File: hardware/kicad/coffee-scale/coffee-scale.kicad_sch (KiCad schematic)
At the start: 4 parts, among them U1 ESP32-S3, U2 HX711

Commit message: Update Schematic
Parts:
- added J1: Screw_Terminal_01x02, symbol Connector:Screw_Terminal_01x02
- added U4: MCP73831-2-MC, Package_DFN_QFN:DFN-8-1EP_3x2mm_P0.5mm_EP1.7x1.4mm, symbol Battery_Management:MCP73831-2-MC
- BT1: value Battery_Cell -> 3.7V
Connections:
- new net: J1.2 (Pin_2), U4.3 (V_{BAT}), U4.4 (V_{BAT})
- new net: U4.1 (V_{DD}), U4.2 (V_{DD})
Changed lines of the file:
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@@
 	(generator_version "8.0")
 	(paper "A4")
+	(junction
+		(at 41.91 123.19)
+		(diameter 0)
+		(color 0 0 0 0)
+	)
 	(wire
 		(pts
@@
 	(wire
 		(pts
+			(xy 31.75 123.19) (xy 41.91 123.19)
+		)
+		(stroke
+			(width 0)
+			(type default)
+		)
+	)
+	(wire
+		(pts
 			(xy 107.95 80.01) (xy 107.95 64.77)
 		)
@@
 	(wire
 		(pts
+			(xy 41.91 123.19) (xy 64.77 123.19)
+		)
+		(stroke
+			(width 0)
+			(type default)
+		)
+	)
+	(wire
+		(pts
 			(xy 191.77 87.63) (xy 191.77 81.28)
 		)
@@
 			(width 0)
 			(type default)
+		)
+	)
+	(wire
+		(pts
+			(xy 64.77 118.11) (xy 58.42 118.11)
+		)
+		(stroke
+			(width 0)
+			(type default)
+		)
+	)
+	(symbol
+		(lib_id "Connector:Screw_Terminal_01x02")
+		(at 36.83 125.73 180)
+		(unit 1)
+		(exclude_from_sim no)
+		(in_bom yes)
+		(on_board yes)
+		(dnp no)
+		(fields_autoplaced yes)
+		(property "Reference" "J1"
+			(at 36.83 116.84 0)
+			(effects
+				(font
+					(size 1.27 1.27)
+				)
+			)
+		)
+		(property "Value" "Screw_Terminal_01x02"
+			(at 36.83 119.38 0)
+			(effects
+				(font
+					(size 1.27 1.27)
+				)
+			)
+		)
+		(property "Footprint" ""
+			(at 36.83 125.73 0)
+			(effects
+				(font
+					(size 1.27 1.27)
+				)
+				(hide yes)
+			)
+		)
+		(property "Datasheet" "~"
+			(at 36.83 125.73 0)
+			(effects
+				(font
+					(size 1.27 1.27)
+				)
+				(hide yes)
+			)
+		)
+		(property "Description" "Generic screw terminal, single row, 01x02, script generated (kicad-library-utils/schlib/autogen/connector/)"
+			(at 36.83 125.73 0)
+			(effects
+				(font
+					(size 1.27 1.27)
+				)
+				(hide yes)
+			)
+		)
+		(pin "2"
+		)
+		(pin "1"
+		)
+		(instances
+			(project ""
+				(path "/26376108-b2bd-4c81-9164-5810df14cd80"
+					(reference "J1")
+					(unit 1)
+				)
+			)
 		)
 	)
@@
 	)
 	(symbol
+		(lib_id "Battery_Management:MCP73831-2-MC")
+		(at 74.93 120.65 180)
+		(unit 1)
+		(exclude_from_sim no)
+		(in_bom yes)
+		(on_board yes)
+		(dnp no)
+		(fields_autoplaced yes)
+		(property "Reference" "U4"
+			(at 92.71 112.6138 0)
+			(effects
+				(font
+					(size 1.27 1.27)
+				)
+			)
+		)
+		(property "Value" "MCP73831-2-MC"
+			(at 92.71 115.1538 0)
+			(effects
+				(font
+					(size 1.27 1.27)
+				)
+			)
+		)
+		(property "Footprint" "Package_DFN_QFN:DFN-8-1EP_3x2mm_P0.5mm_EP1.7x1.4mm"
+			(at 73.66 114.3 0)
+			(effects
+				(font
+					(size 1.27 1.27)
+					(italic yes)
+				)
+				(justify left)
+				(hide yes)
+			)
+		)
+		(property "Datasheet" "http://ww1.microchip.com/downloads/en/DeviceDoc/20001984g.pdf"
+			(at 78.74 119.38 0)
+			(effects
+				(font
+					(size 1.27 1.27)
+				)
+				(hide yes)
+			)
+		)
+		(property "Description" "Single cell, Li-Ion/Li-Po charge management controller, 4.20V, Tri-State Status Output, in DFN-8 package"
+			(at 74.93 120.65 0)
+			(effects
+				(font
+					(size 1.27 1.27)
+				)
+				(hide yes)
+			)
+		)
+		(pin "3"
+		)
+		(pin "8"
+		)
+		(pin "5"
+		)
+		(pin "2"
+		)
+		(pin "6"
+		)
+		(pin "1"
+		)
+		(pin "7"
+		)
+		(pin "4"
+		)
+		(instances
+			(project ""
+				(path "/26376108-b2bd-4c81-9164-5810df14cd80"
+					(reference "U4")
+					(unit 1)
+				)
+			)
+		)
+	)
+	(symbol
 		(lib_id "MCU_Espressif:ESP32-S3")
 		(at 146.05 90.17 0)
@@
 	(symbol
 		(lib_id "Device:Battery_Cell")
-		(at 196.85 106.68 0)
+		(at 52.07 135.89 0)
 		(unit 1)
 		(exclude_from_sim no)
@@
 		(fields_autoplaced yes)
 		(property "Reference" "BT1"
-			(at 200.66 103.5684 0)
+			(at 55.88 132.7784 0)
 			(effects
 				(font
@@
 			)
 		)
-		(property "Value" "Battery_Cell"
-			(at 200.66 106.1084 0)
+		(property "Value" "3.7V"
+			(at 55.88 135.3184 0)
 			(effects
 				(font
@@
 		)
 		(property "Footprint" ""
-			(at 196.85 105.156 90)
+			(at 52.07 134.366 90)
 			(effects
 				(font
@@
 		)
 		(property "Datasheet" "~"
-			(at 196.85 105.156 90)
+			(at 52.07 134.366 90)
 			(effects
 				(font
@@
 		)
 		(property "Description" "Single-cell battery"
-			(at 196.85 106.68 0)
+			(at 52.07 135.89 0)
 			(effects
 				(font
@@
 		)
 		(instances
-			(project ""
+			(project "coffee-scale"
 				(path "/26376108-b2bd-4c81-9164-5810df14cd80"
 					(reference "BT1")

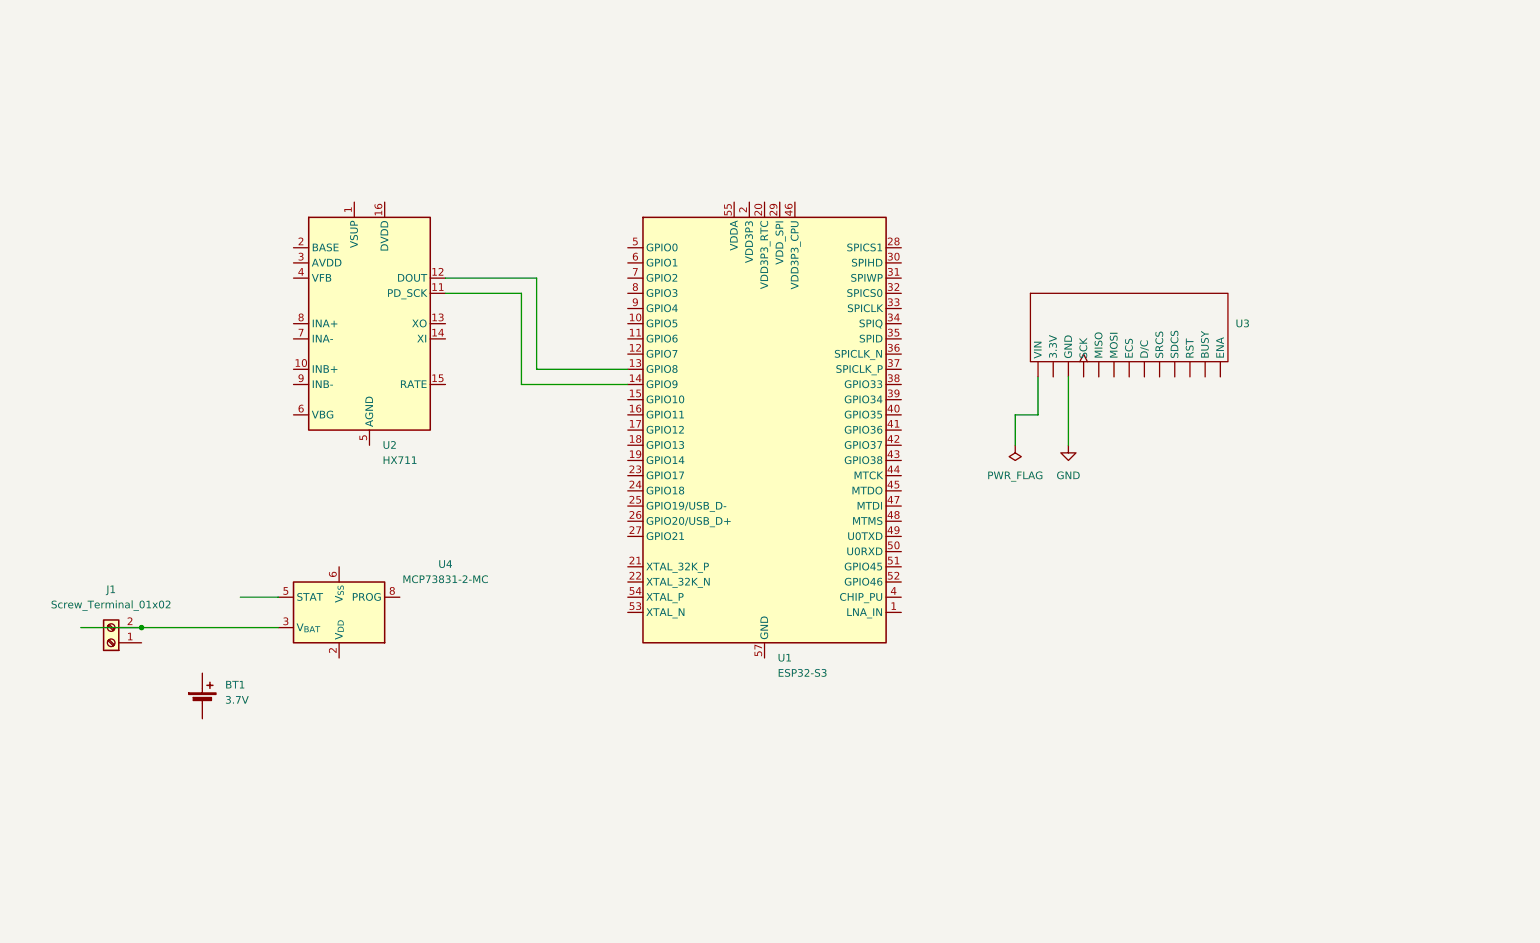
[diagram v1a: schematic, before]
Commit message: Added load cell symbol and made connection to the HX711
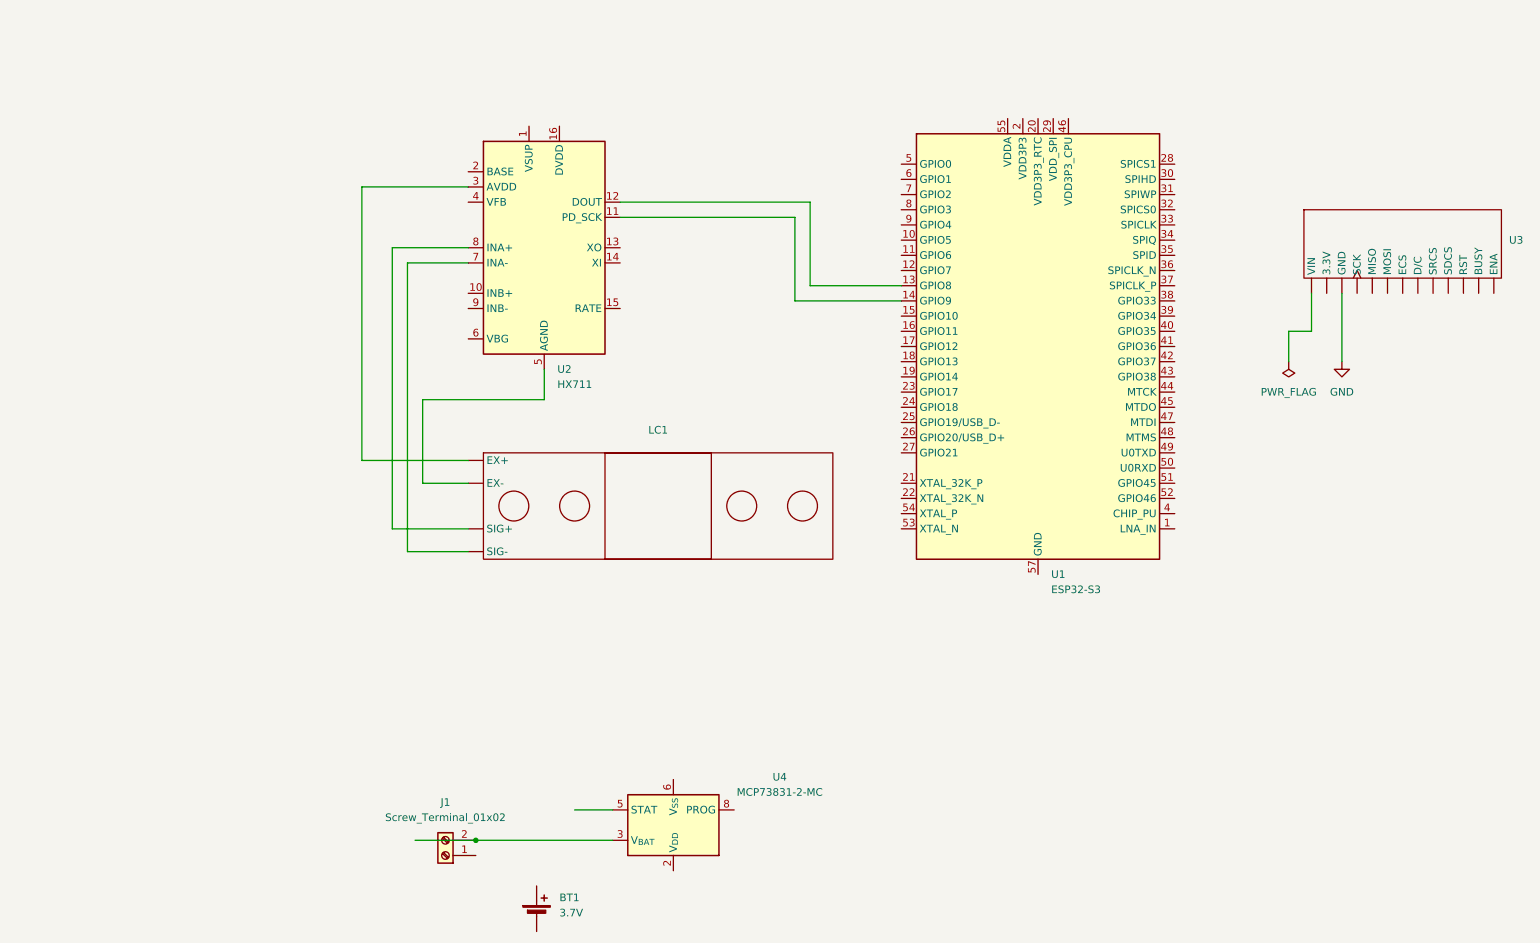
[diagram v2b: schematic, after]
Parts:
- added LC1: ~, symbol Custom:4540
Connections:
- net at U2.3 (AVDD): now also LC1. (SIG-)
- net at U2.5 (AGND): now also LC1. (SIG-)
- net at U2.7 (INA-): now also LC1. (SIG-)
- net at U2.8 (INA+): now also LC1. (SIG-)
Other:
- moved on the sheet: BT1, J1, U1, U2, U3, U4

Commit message: Update on KiCad
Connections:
- net GND: now also LC1. (SIG-), U1.57 (GND), U2.5 (AGND)
- net at U1.40 (GPIO35): now also U3. (VIN)
- net at U1.41 (GPIO36): now also U3. (VIN)
- net at U1.42 (GPIO37): now also U3. (VIN)
- net at U2.3 (AVDD): no longer LC1. (SIG-)
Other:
- moved on the sheet: BT1, J1, LC1, U1, U2, U3, U4

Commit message: Update Schematic
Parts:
- added C1, C2: 4.7uF, symbol Device:C
- added D1: LED, symbol Device:LED
- added JP1: SolderJumper_2_Bridged, symbol Jumper:SolderJumper_2_Bridged
- added R1: 2k, symbol Device:R
- added R2: R, symbol Device:R
- added R3: 1k, symbol Device:R
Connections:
- net GND: now also J1.1 (Pin_1), U4.6 (V_{SS}), C1.2, C2.2, R1.2, R2.2
- net +BATT: now reaches J1.2 (Pin_2), U4.3 (V_{BAT}), U4.4 (V_{BAT})
- net +BATT: now also U4.5 (STAT), C1.1, D1.1 (K)
- net VBUS: now reaches U4.1 (V_{DD}), U4.2 (V_{DD})
- net VBUS: now also C2.1, R3.2
- net at U4.8 (PROG): now also JP1.2 (B), R2.1
- new net: JP1.1 (A), R1.1
- new net: D1.2 (A), R3.1
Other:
- moved on the sheet: BT1

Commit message: Update Schematic
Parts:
- removed BT1: 3.7V, symbol Device:Battery_Cell
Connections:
- net at U1.38 (GPIO33): now also U3. (VIN)
- net at U1.39 (GPIO34): now also U3. (VIN)
- net at U1.43 (GPIO38): now also U3. (VIN)
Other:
- note added: "LiPo Battery Circuit"
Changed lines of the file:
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@@
+	(wire
+		(pts
+			(xy 195.58 48.26) (xy 195.58 60.96)
+		)
+		(stroke
+			(width 0)
+			(type default)
+		)
+	)
 	(wire
 		(pts
@@
 	(wire
 		(pts
+			(xy 195.58 60.96) (xy 154.94 60.96)
+		)
+		(stroke
+			(width 0)
+			(type default)
+		)
+	)
+	(wire
+		(pts
 			(xy 26.67 52.07) (xy 36.83 52.07)
 		)
@@
 	(wire
 		(pts
+			(xy 203.2 71.12) (xy 154.94 71.12)
+		)
+		(stroke
+			(width 0)
+			(type default)
+		)
+	)
+	(wire
+		(pts
 			(xy 36.83 100.33) (xy 26.67 100.33)
 		)
@@
 	(wire
 		(pts
+			(xy 193.04 58.42) (xy 154.94 58.42)
+		)
+		(stroke
+			(width 0)
+			(type default)
+		)
+	)
+	(wire
+		(pts
 			(xy 24.13 49.53) (xy 36.83 49.53)
 		)
@@
 	(wire
 		(pts
+			(xy 193.04 48.26) (xy 193.04 58.42)
+		)
+		(stroke
+			(width 0)
+			(type default)
+		)
+	)
+	(wire
+		(pts
 			(xy 111.76 142.24) (xy 105.41 142.24)
 		)
@@
 	(wire
 		(pts
+			(xy 203.2 48.26) (xy 203.2 71.12)
+		)
+		(stroke
+			(width 0)
+			(type default)
+		)
+	)
+	(wire
+		(pts
 			(xy 76.2 137.16) (xy 76.2 154.94)
 		)
@@
 			(width 0)
 			(type default)
+		)
+	)
+	(rectangle
+		(start 36.83 128.905)
+		(end 142.875 173.355)
+		(stroke
+			(width 0)
+			(type dot)
+		)
+		(fill
+			(type none)
+		)
+	)
+	(text "LiPo Battery Circuit"
+		(exclude_from_sim no)
+		(at 46.736 130.81 0)
+		(effects
+			(font
+				(size 1.27 1.27)
+			)
 		)
 	)
@@
 					(unit 1)
 				)
-			)
-		)
-	)
-	(symbol
-		(lib_id "Device:Battery_Cell")
-		(at 54.61 116.84 0)
-		(unit 1)
-		(exclude_from_sim no)
-		(in_bom yes)
-		(on_board yes)
-		(dnp no)
-		(fields_autoplaced yes)
-		(property "Reference" "BT1"
-			(at 58.42 113.7284 0)
-			(effects
-				(font
-					(size 1.27 1.27)
-				)
-				(justify left)
-			)
-		)
-		(property "Value" "3.7V"
-			(at 58.42 116.2684 0)
-			(effects
-				(font
-					(size 1.27 1.27)
-				)
-				(justify left)
-			)
-		)
-		(property "Footprint" ""
-			(at 54.61 115.316 90)
-			(effects
-				(font
-					(size 1.27 1.27)
-				)
-				(hide yes)
-			)
-		)
-		(property "Datasheet" "~"
-			(at 54.61 115.316 90)
-			(effects
-				(font
-					(size 1.27 1.27)
-				)
-				(hide yes)
-			)
-		)
-		(property "Description" "Single-cell battery"
-			(at 54.61 116.84 0)
-			(effects
-				(font
-					(size 1.27 1.27)
-				)
-				(hide yes)
-			)
-		)
-		(pin "2"
-		)
-		(pin "1"
-		)
-		(instances
-			(project "coffee-scale"
-				(path "/26376108-b2bd-4c81-9164-5810df14cd80"
-					(reference "BT1")
-					(unit 1)
-				)

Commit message: Update Schematic
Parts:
- removed C1, C2: 4.7uF, symbol Device:C
- removed D1: LED, symbol Device:LED
- removed J1: Screw_Terminal_01x02, symbol Connector:Screw_Terminal_01x02
- removed JP1: SolderJumper_2_Bridged, symbol Jumper:SolderJumper_2_Bridged
- removed R1: 2k, symbol Device:R
- removed R2: R, symbol Device:R
- removed R3: 1k, symbol Device:R
- removed U4: MCP73831-2-MC, Package_DFN_QFN:DFN-8-1EP_3x2mm_P0.5mm_EP1.7x1.4mm, symbol Battery_Management:MCP73831-2-MC
- added C3, C4: 4.7uF, symbol Device:C
- added D2: LED, symbol Device:LED
- added J1: JS2, symbol Connector:Conn_01x02_Pin
- added JP2: SolderJumper_2_Bridged, symbol Jumper:SolderJumper_2_Bridged
- added R4: 1k, symbol Device:R
- added R5: R, symbol Device:R
- added R6: 2k, symbol Device:R
- added U5: MCP73831-2-MC, Package_DFN_QFN:DFN-8-1EP_3x2mm_P0.5mm_EP1.7x1.4mm, symbol Battery_Management:MCP73831-2-MC
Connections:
- net +BATT: now also C3.1, D2.1 (K), J1.1 (Pin_1), U5.3 (V_{BAT}), U5.4 (V_{BAT}), U5.5 (STAT)
- net GND: now also C3.2, C4.2, J1.2 (Pin_2), R5.2, R6.2, U5.6 (V_{SS})
- net VBUS: now also C4.1, R4.2, U5.1 (V_{DD}), U5.2 (V_{DD})
- new net: D2.2 (A), R4.1
- new net: JP2.2 (B), R5.1, U5.8 (PROG)
- new net: JP2.1 (A), R6.1
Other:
- added sheet Lipo Battery Charger (untitled.kicad_sch)

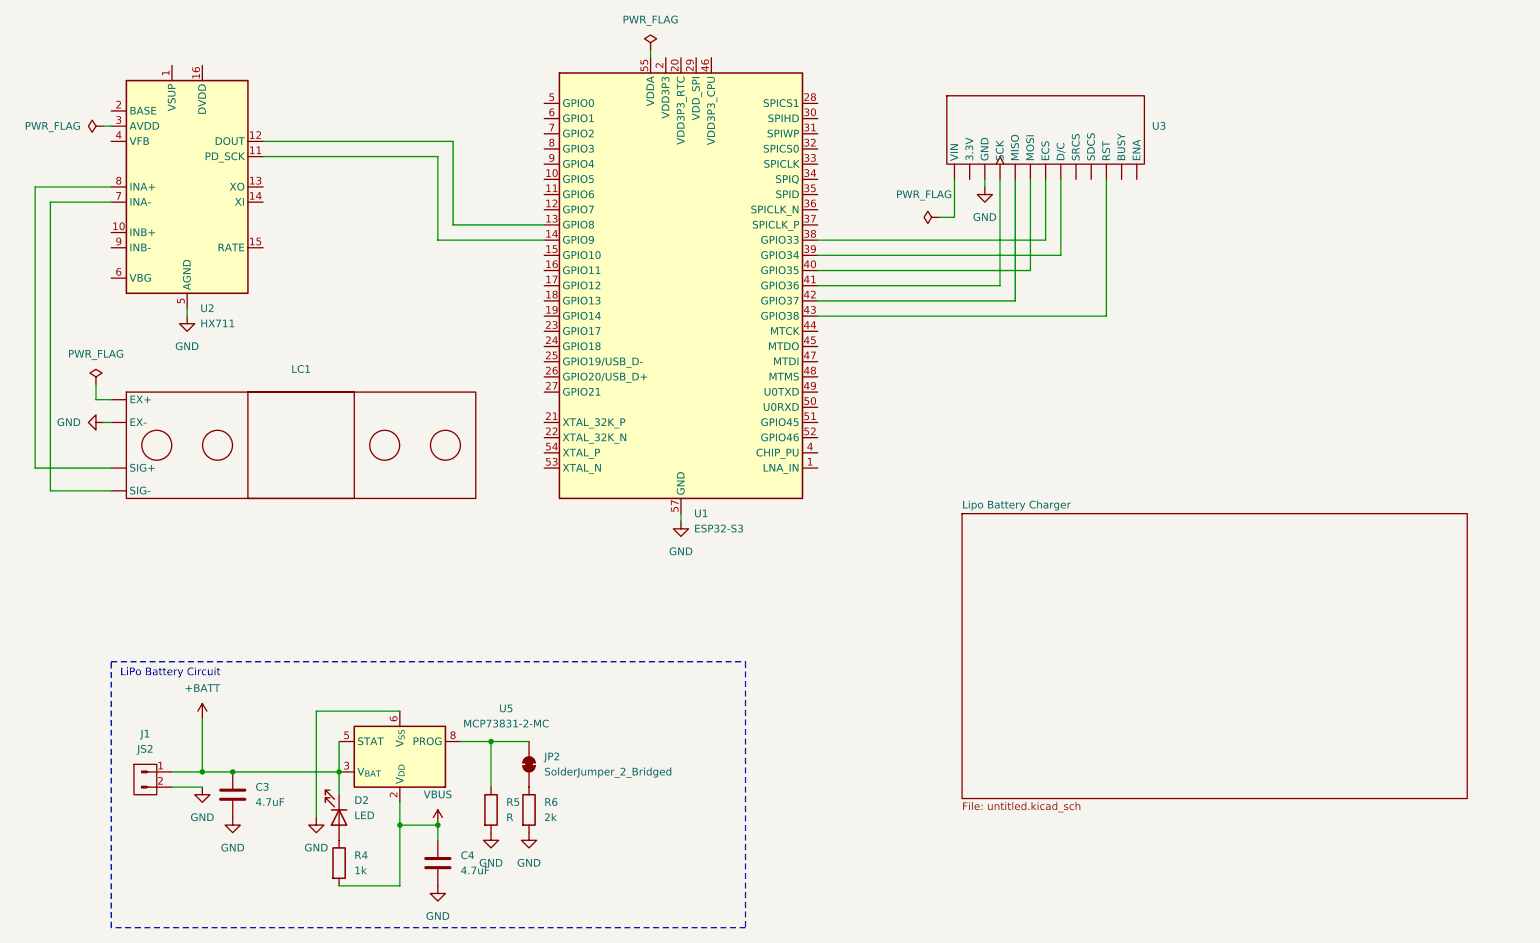
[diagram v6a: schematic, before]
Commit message: Update Schematic
Creates individual sheets for different major moving part sections
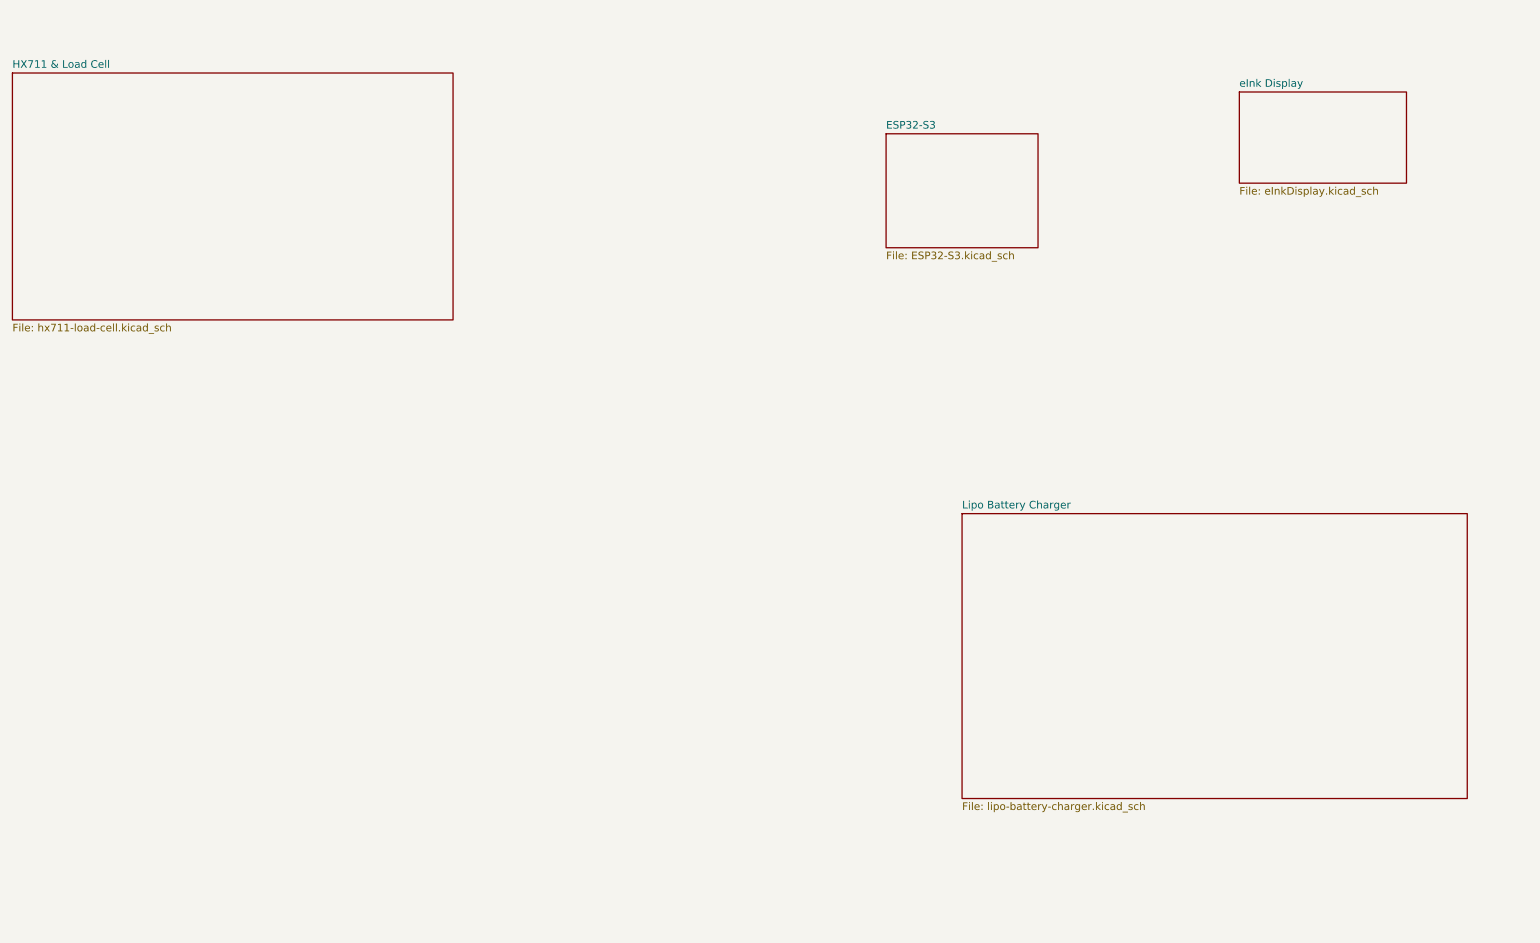
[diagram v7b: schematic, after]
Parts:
- removed C3, C4: 4.7uF, symbol Device:C
- removed D2: LED, symbol Device:LED
- removed J1: JS2, symbol Connector:Conn_01x02_Pin
- removed JP2: SolderJumper_2_Bridged, symbol Jumper:SolderJumper_2_Bridged
- removed LC1: ~, symbol Custom:4540
- removed R4: 1k, symbol Device:R
- removed R5: R, symbol Device:R
- removed R6: 2k, symbol Device:R
- removed U1: ESP32-S3, Package_DFN_QFN:QFN-56-1EP_7x7mm_P0.4mm_EP4x4mm, symbol MCU_Espressif:ESP32-S3
- removed U2: HX711, Package_SO:SOP-16_3.9x9.9mm_P1.27mm, symbol Analog_ADC:HX711
- removed U3: ~, symbol Custom:UC8151D
- removed U5: MCP73831-2-MC, Package_DFN_QFN:DFN-8-1EP_3x2mm_P0.5mm_EP1.7x1.4mm, symbol Battery_Management:MCP73831-2-MC
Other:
- added sheet ESP32-S3 (ESP32-S3.kicad_sch)
- added sheet HX711 & Load Cell (hx711-load-cell.kicad_sch)
- added sheet eInk Display (eInkDisplay.kicad_sch)
- sheet Lipo Battery Charger: file untitled.kicad_sch -> lipo-battery-charger.kicad_sch
- note removed: "LiPo Battery Circuit"
